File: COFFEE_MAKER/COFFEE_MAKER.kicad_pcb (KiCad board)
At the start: 2 copper layers, 131.4 x 99.7 mm, 55 parts, among them J1 Conn_01x03_Pin, J2 Conn_01x06, J3 Conn_01x03_Pin, J4 Screw_Terminal_01x02, J5 USB_C_Receptacle_USB2.0_16P, J6 Barrel_Jack, J7 Conn_01x04, Q1 BC850, SW5 Reset, SW6 Boot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

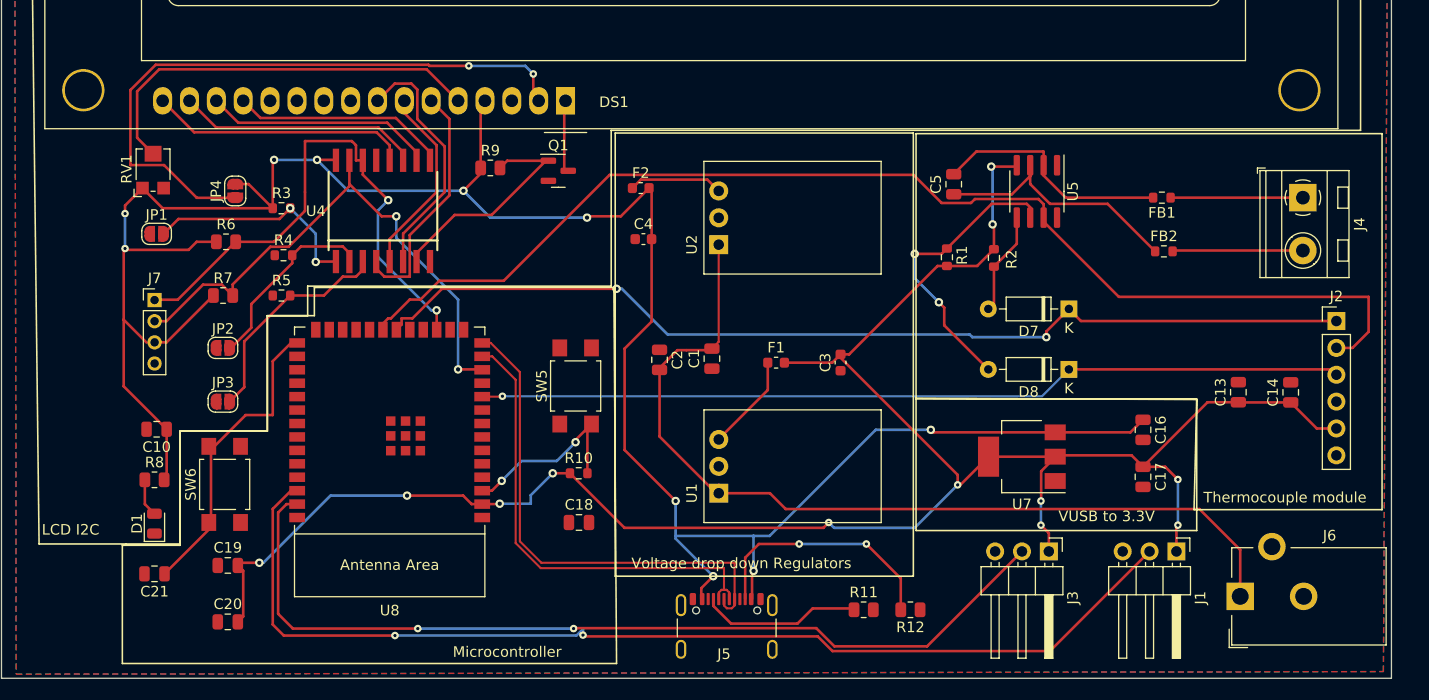
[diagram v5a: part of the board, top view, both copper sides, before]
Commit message: pcb finalized, manufacturing folder finalized, BOM& slides in submission folder finalized
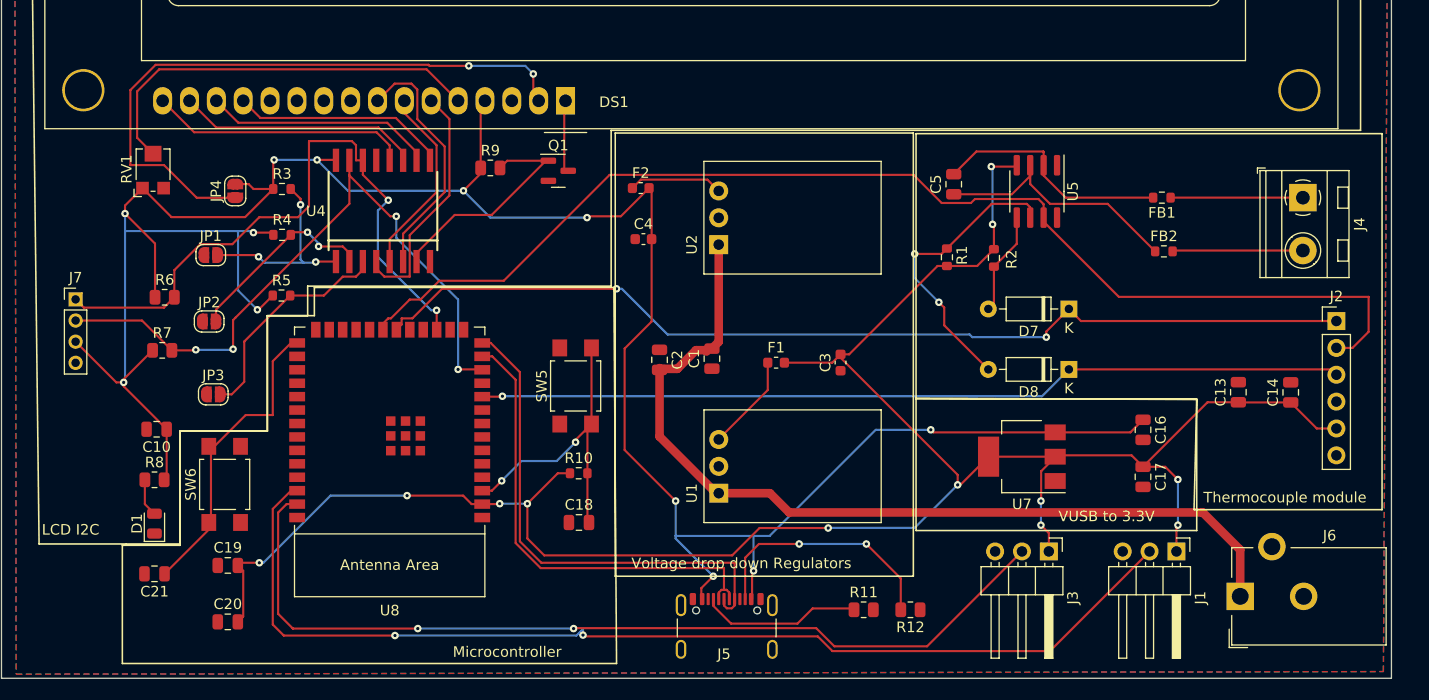
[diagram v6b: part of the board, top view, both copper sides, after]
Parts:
- moved R6 7.82 mm to (113.2, 83.3)
- moved R7 7.75 mm to (113.0, 88.4)
- moved J7 7.47 mm to (104.8, 83.5)
- moved JP1 5.50 mm to (117.6, 79.4)
- moved JP2 2.82 mm to (117.4, 85.6)
- moved R4 1.93 mm to (124.3, 77.5)
- moved R3 1.82 mm to (124.3, 73.1)
- moved JP3 1.14 mm to (117.8, 92.5)
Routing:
- net +5V: track 220.8 -> 244.6 mm, vias 10 -> 12
- net LCD_sda: track 52.8 -> 64.9 mm, vias 2 -> 4
- net Net-(U8-EN): track 17.9 -> 29.8 mm
- net LCD_scl: track 51.4 -> 61.5 mm
- net +3V3: track 196.9 -> 202.9 mm
- net Net-(JP1-B): track 21.0 -> 19.0 mm, vias 2 -> 3
- net V_ALL+: track 86.2 -> 85.5 mm
- net Net-(JP2-B): track 18.1 -> 18.6 mm, vias 0 -> 2
